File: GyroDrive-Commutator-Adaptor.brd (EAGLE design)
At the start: 127 x 76.2 mm, 24 parts, among them U1 HALL, U2 PCA9517, U3 5V, U4 2.5V, U5 INA2141U, U6 INA2141U, U7 INA2141U, X1 NORCOMP-DB25-SMD-MALE

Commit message: Shortened board by 0.75 inches to make room for DB25-Dale adapter
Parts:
- moved U1 19.0 mm to (102.9, 38.1)
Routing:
- net AGND: track 116.9 -> 97.8 mm
- net HALL0: track 105.4 -> 86.4 mm
- net HALL1: track 109.3 -> 90.6 mm
- net V+_HALL: track 67.0 -> 48.5 mm
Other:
- board size 127 x 76.2 mm -> 108 x 76.2 mm
- board text added: "GyroDrive-Commutator Adapter Version 1 Michael Stetner Fee Lab, 2016"
- board text removed: "Fee lab, 2013"
- board text removed: "Tatsuo Okubo"
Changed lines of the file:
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@@
 <plain>
 <wire x1="0" y1="2.54" x2="2.54" y2="0" width="0" layer="20" curve="90"/>
-<wire x1="2.54" y1="0" x2="48.26" y2="0" width="0" layer="20"/>
-<wire x1="48.26" y1="0" x2="50.8" y2="2.54" width="0" layer="20" curve="90"/>
-<wire x1="50.8" y1="2.54" x2="50.8" y2="27.94" width="0" layer="20"/>
-<wire x1="50.8" y1="27.94" x2="53.34" y2="30.48" width="0" layer="20" curve="-90"/>
-<wire x1="53.34" y1="30.48" x2="124.46" y2="30.48" width="0" layer="20"/>
-<wire x1="124.46" y1="30.48" x2="127" y2="33.02" width="0" layer="20" curve="90"/>
-<wire x1="127" y1="33.02" x2="127" y2="43.18" width="0" layer="20"/>
-<wire x1="127" y1="43.18" x2="124.46" y2="45.72" width="0" layer="20" curve="90"/>
-<wire x1="124.46" y1="45.72" x2="53.34" y2="45.72" width="0" layer="20"/>
-<wire x1="53.34" y1="45.72" x2="50.8" y2="48.26" width="0" layer="20" curve="-90"/>
-<wire x1="50.8" y1="48.26" x2="50.8" y2="73.66" width="0" layer="20"/>
-<wire x1="50.8" y1="73.66" x2="48.26" y2="76.2" width="0" layer="20" curve="90"/>
-<wire x1="48.26" y1="76.2" x2="2.54" y2="76.2" width="0" layer="20"/>
+<wire x1="2.54" y1="0" x2="29.21" y2="0" width="0" layer="20"/>
+<wire x1="29.21" y1="0" x2="31.75" y2="2.54" width="0" layer="20" curve="90"/>
+<wire x1="31.75" y1="2.54" x2="31.75" y2="27.94" width="0" layer="20"/>
+<wire x1="31.75" y1="27.94" x2="34.29" y2="30.48" width="0" layer="20" curve="-90"/>
+<wire x1="34.29" y1="30.48" x2="105.41" y2="30.48" width="0" layer="20"/>
+<wire x1="105.41" y1="30.48" x2="107.95" y2="33.02" width="0" layer="20" curve="90"/>
+<wire x1="107.95" y1="33.02" x2="107.95" y2="43.18" width="0" layer="20"/>
+<wire x1="107.95" y1="43.18" x2="105.41" y2="45.72" width="0" layer="20" curve="90"/>
+<wire x1="105.41" y1="45.72" x2="34.29" y2="45.72" width="0" layer="20"/>
+<wire x1="34.29" y1="45.72" x2="31.75" y2="48.26" width="0" layer="20" curve="-90"/>
+<wire x1="31.75" y1="48.26" x2="31.75" y2="73.66" width="0" layer="20"/>
+<wire x1="31.75" y1="73.66" x2="29.21" y2="76.2" width="0" layer="20" curve="90"/>
+<wire x1="29.21" y1="76.2" x2="2.54" y2="76.2" width="0" layer="20"/>
 <wire x1="2.54" y1="76.2" x2="0" y2="73.66" width="0" layer="20" curve="90"/>
 <wire x1="0" y1="73.66" x2="0" y2="2.54" width="0" layer="20"/>
-<text x="49.53" y="2.54" size="1.778" layer="21" rot="R90">Fee lab, 2013</text>
-<text x="45.72" y="2.54" size="1.778" layer="21" rot="R90">Tatsuo Okubo</text>
+<text x="15.8242" y="42.1386" size="1.778" layer="22" rot="MR270" align="center">GyroDrive-Commutator Adapter
+Version 1
+Michael Stetner
+Fee Lab, 2016</text>
 </plain>
 <attributes>
@@
 </element>
 <element name="X2" library="pinhead" package="2X08" value="" x="27.178" y="38.1" rot="R90"/>
-<element name="U1" library="elm" package="HALL_ON_SIDE" value="HALL" x="121.92" y="38.1"/>
+<element name="U1" library="elm" package="HALL_ON_SIDE" value="HALL" x="102.87" y="38.1"/>
 <element name="U7" library="burr-brown" package="SO16-1" value="INA2141U" x="14.986" y="49.3014" rot="R180">
 <attribute name="OC_NEWARK" value="74C9853" x="-4.064" y="87.4014" size="1.778" layer="27" rot="R180" display="off"/>
@@
 <signal name="HALL0">
 <contactref element="U1" pad="D"/>
-<wire x1="52.07" y1="36.83" x2="118.11" y2="36.83" width="0.3048" layer="1"/>
-<wire x1="118.11" y1="36.83" x2="119.3038" y2="35.6362" width="0.254" layer="1"/>
-<wire x1="119.3038" y1="35.6362" x2="120.396" y2="35.6362" width="0.254" layer="1"/>
+<wire x1="52.07" y1="36.83" x2="99.3902" y2="36.8046" width="0.3048" layer="1"/>
+<wire x1="99.3902" y1="36.8046" x2="100.584" y2="35.6108" width="0.254" layer="1"/>
+<wire x1="100.584" y1="35.6108" x2="101.346" y2="35.6362" width="0.254" layer="1"/>
 <contactref element="U7" pad="16"/>
 <wire x1="52.07" y1="36.83" x2="37.719" y2="36.83" width="0.254" layer="1"/>
@@
 <contactref element="R1" pad="1"/>
 <contactref element="U1" pad="C"/>
-<wire x1="61.595" y1="34.163" x2="121.793" y2="34.163" width="0.3048" layer="1"/>
-<wire x1="121.793" y1="34.163" x2="123.19" y2="35.56" width="0.3048" layer="1"/>
-<wire x1="123.19" y1="35.56" x2="123.571" y2="35.56" width="0.3048" layer="1"/>
-<wire x1="123.571" y1="35.56" x2="123.5964" y2="35.5854" width="0.3048" layer="1"/>
+<wire x1="61.595" y1="34.163" x2="103.0732" y2="34.1376" width="0.3048" layer="1"/>
+<wire x1="103.0732" y1="34.1376" x2="104.4702" y2="35.5346" width="0.3048" layer="1"/>
+<wire x1="104.4702" y1="35.5346" x2="104.8512" y2="35.5346" width="0.3048" layer="1"/>
+<wire x1="104.8512" y1="35.5346" x2="104.5464" y2="35.5854" width="0.3048" layer="1"/>
 <wire x1="61.595" y1="34.163" x2="57.404" y2="34.163" width="0.254" layer="1"/>
 <wire x1="57.404" y1="34.163" x2="57.277" y2="34.29" width="0.254" layer="1"/>
@@
 <contactref element="U1" pad="B"/>
 <contactref element="U7" pad="15"/>
-<wire x1="122.809" y1="38.1" x2="122.809" y2="40.1066" width="0.254" layer="1"/>
-<wire x1="122.809" y1="40.1066" x2="122.1486" y2="40.767" width="0.254" layer="1"/>
-<wire x1="122.1486" y1="40.767" x2="40.3098" y2="40.767" width="0.254" layer="1"/>
+<wire x1="103.759" y1="38.1" x2="104.0892" y2="40.0812" width="0.254" layer="1"/>
+<wire x1="104.0892" y1="40.0812" x2="103.4288" y2="40.7416" width="0.254" layer="1"/>
+<wire x1="103.4288" y1="40.7416" x2="40.3098" y2="40.767" width="0.254" layer="1"/>
 <wire x1="18.1356" y1="44.5516" x2="18.161" y2="44.5262" width="0.254" layer="1"/>
 <via x="40.3098" y="40.767" extent="1-16" drill="0.6"/>
@@
 <contactref element="U7" pad="12"/>
 <contactref element="U5" pad="5"/>
-<wire x1="121.0818" y1="38.1" x2="46.5582" y2="38.1" width="0.254" layer="1"/>
+<wire x1="102.0318" y1="38.1" x2="46.5582" y2="38.1" width="0.254" layer="1"/>
 <polygon width="0.4064" layer="15">
 <vertex x="0" y="0"/>
@@
 <vertex x="29.5656" y="43.18"/>
 <vertex x="29.5656" y="76.2"/>
-<vertex x="50.8" y="76.2"/>
-<vertex x="50.8" y="45.72"/>
-<vertex x="127" y="45.72"/>
-<vertex x="127" y="30.48"/>
-<vertex x="50.8" y="30.48"/>
-<vertex x="50.8" y="0"/>
+<vertex x="31.75" y="76.2"/>
+<vertex x="31.75" y="45.72"/>
+<vertex x="107.95" y="45.72"/>
+<vertex x="107.95" y="30.48"/>
+<vertex x="31.75" y="30.48"/>
+<vertex x="31.75" y="0"/>
 </polygon>
 <contactref element="X1" pad="P$10"/>
@@
 </board>
 </drawing>
+<compatibility>
+<note version="6.3" minversion="6.2.2" severity="warning">
+Since Version 6.2.2 text objects can contain more than one line,
+which will not be processed correctly with this version.
+</note>
+</compatibility>
 </eagle>

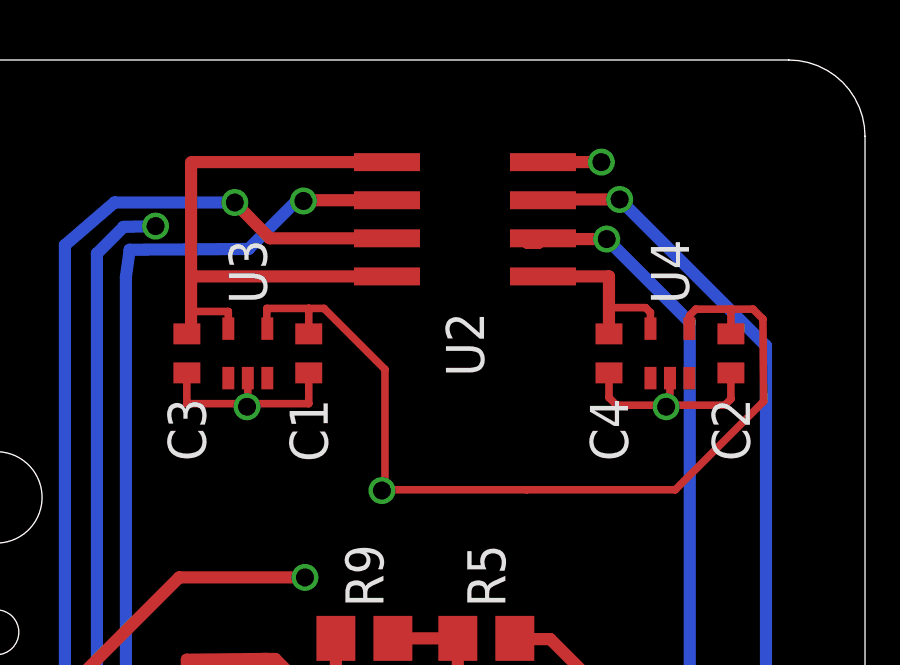
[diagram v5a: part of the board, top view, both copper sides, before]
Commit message: I2C pull-up resistors added
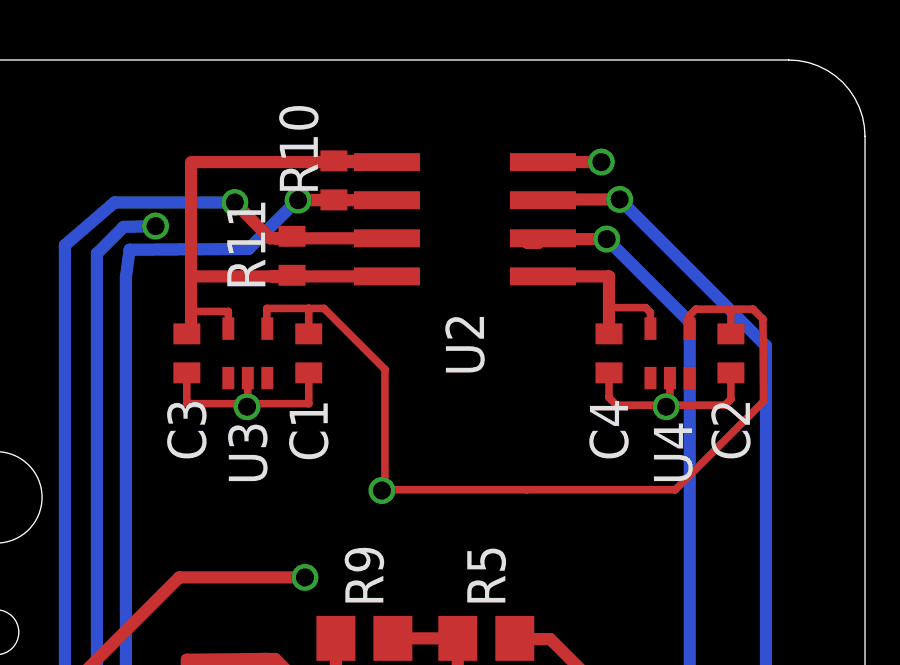
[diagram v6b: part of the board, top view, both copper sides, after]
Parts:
- added R10, R11: 10k, resistor:R0402
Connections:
- net +5V: now also R10.2, R11.2
- net SCL_RIG: now also R11.1
- net SDA_RIG: now also R10.1
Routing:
- net +5V: track 20.7 -> 22.1 mm
- net SDA_RIG: track 50.1 -> 51.3 mm
- net SCL_RIG: track 53.5 -> 54.1 mm
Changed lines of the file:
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@@
 <layer number="27" name="tValues" color="7" fill="1" visible="no" active="yes"/>
 <layer number="28" name="bValues" color="7" fill="1" visible="no" active="yes"/>
-<layer number="29" name="tStop" color="7" fill="3" visible="no" active="yes"/>
+<layer number="29" name="tStop" color="7" fill="3" visible="yes" active="yes"/>
 <layer number="30" name="bStop" color="7" fill="6" visible="yes" active="yes"/>
 <layer number="31" name="tCream" color="7" fill="4" visible="yes" active="yes"/>
@@
 </class>
 </classes>
-<designrules name="OSHPark-4layer">
+<designrules name="OSHPark-4layer *">
 <description language="de">&lt;b&gt;EAGLE Design Rules&lt;/b&gt;
 &lt;p&gt;
@@
 <param name="mlMinCreamFrame" value="0mil"/>
 <param name="mlMaxCreamFrame" value="0mil"/>
-<param name="mlViaStopLimit" value="0mil"/>
+<param name="mlViaStopLimit" value="30mil"/>
 <param name="srRoundness" value="0"/>
 <param name="srMinRoundness" value="0mil"/>
@@
 <element name="X1" library="michael-stetner" package="190-025-163R001" value="NORCOMP-DB25-SMD-MALE" x="0" y="38.1" rot="R90"/>
 <element name="U3" library="michael-stetner" package="SC70" value="5V" x="11.176" y="66.421" smashed="yes">
-<attribute name="NAME" x="11.176" y="68.072" size="1.27" layer="25" rot="R90" align="center-left"/>
+<attribute name="NAME" x="11.176" y="62.0268" size="1.27" layer="25" rot="R90" align="center-left"/>
 <attribute name="VALUE" x="10.414" y="66.167" size="0.4064" layer="27"/>
 </element>
@@
 </element>
 <element name="U4" library="michael-stetner" package="SC70" value="2.5V" x="25.2476" y="66.421" smashed="yes">
-<attribute name="NAME" x="25.2476" y="68.072" size="1.27" layer="25" rot="R90" align="center-left"/>
+<attribute name="NAME" x="25.3492" y="62.0268" size="1.27" layer="25" rot="R90" align="center-left"/>
 <attribute name="VALUE" x="24.4856" y="66.167" size="0.4064" layer="27"/>
 </element>
@@
 <attribute name="NAME" x="23.2156" y="64.9224" size="1.27" layer="25" rot="R270" align="center-left"/>
 <attribute name="VALUE" x="21.3106" y="67.056" size="1.27" layer="27" rot="R270"/>
+</element>
+<element name="R10" library="resistor" package="R0402" value="10k" x="14.0462" y="72.1868" smashed="yes" rot="R90">
+<attribute name="NAME" x="13.5128" y="73.2282" size="1.27" layer="25" rot="R270" align="top-center"/>
+<attribute name="VALUE" x="15.9512" y="71.5518" size="1.27" layer="27" rot="R90"/>
+</element>
+<element name="R11" library="resistor" package="R0402" value="10k" x="12.6492" y="69.6722" smashed="yes" rot="R270">
+<attribute name="NAME" x="11.7602" y="68.5038" size="1.27" layer="25" rot="R90"/>
+<attribute name="VALUE" x="10.7442" y="70.3072" size="1.27" layer="27" rot="R270"/>
 </element>
 </elements>
@@
 <contactref element="U3" pad="5"/>
 <contactref element="C3" pad="1"/>
-<wire x1="15.815" y1="72.7964" x2="9.398" y2="72.7964" width="0.4064" layer="1"/>
+<wire x1="15.815" y1="72.7964" x2="14.7574" y2="72.7964" width="0.4064" layer="1"/>
+<wire x1="14.7574" y1="72.7964" x2="9.398" y2="72.7964" width="0.4064" layer="1"/>
 <wire x1="9.398" y1="72.7964" x2="9.286" y2="72.7964" width="0.4064" layer="1"/>
-<wire x1="15.815" y1="68.9864" x2="9.286" y2="68.9864" width="0.4064" layer="1"/>
+<wire x1="15.815" y1="68.9864" x2="11.9888" y2="68.9864" width="0.4064" layer="1"/>
+<wire x1="11.9888" y1="68.9864" x2="9.286" y2="68.9864" width="0.4064" layer="1"/>
 <wire x1="9.286" y1="68.9864" x2="9.286" y2="72.6844" width="0.4064" layer="1"/>
 <wire x1="9.286" y1="72.6844" x2="9.398" y2="72.7964" width="0.4064" layer="1"/>
@@
 <wire x1="10.526" y1="67.246" x2="10.526" y2="67.818" width="0.254" layer="1"/>
 <wire x1="10.526" y1="67.818" x2="9.286" y2="67.818" width="0.254" layer="1"/>
+<contactref element="R10" pad="2"/>
+<contactref element="R11" pad="2"/>
+<wire x1="14.0462" y1="72.8368" x2="14.7574" y2="72.8368" width="0.4064" layer="1"/>
+<wire x1="14.7574" y1="72.8368" x2="14.7574" y2="72.7964" width="0.4064" layer="1"/>
+<wire x1="12.6492" y1="69.0222" x2="12.6238" y2="68.9714" width="0.4064" layer="1"/>
+<wire x1="12.6238" y1="68.9714" x2="11.9888" y2="68.9864" width="0.4064" layer="1"/>
 </signal>
 <signal name="SDA_BIRD">
@@
 <wire x1="6.1214" y1="33.9344" x2="7.112" y2="33.9344" width="0.4064" layer="16"/>
 <wire x1="7.112" y1="33.9344" x2="7.112" y2="68.961" width="0.4064" layer="16"/>
-<wire x1="15.815" y1="71.5264" x2="13.0556" y2="71.5264" width="0.4064" layer="1"/>
-<wire x1="13.0556" y1="71.5264" x2="13.0302" y2="71.501" width="0.4064" layer="1"/>
-<via x="13.0302" y="71.501" extent="1-16" drill="0.6"/>
-<wire x1="13.0302" y1="71.501" x2="12.8016" y2="71.501" width="0.4064" layer="16"/>
+<wire x1="15.815" y1="71.5264" x2="12.8524" y2="71.5264" width="0.4064" layer="1"/>
+<via x="12.8524" y="71.5264" extent="1-16" drill="0.6"/>
+<wire x1="12.8524" y1="71.5264" x2="12.8016" y2="71.501" width="0.4064" layer="16"/>
 <wire x1="12.8016" y1="71.501" x2="11.2014" y2="69.9008" width="0.4064" layer="16"/>
 <wire x1="11.2014" y1="69.9008" x2="7.239" y2="69.8754" width="0.4064" layer="16"/>
 <wire x1="7.239" y1="69.8754" x2="7.112" y2="68.961" width="0.4064" layer="16"/>
+<contactref element="R10" pad="1"/>
+<wire x1="14.0462" y1="71.5368" x2="13.0302" y2="71.5368" width="0.4064" layer="1"/>
+<wire x1="13.0302" y1="71.5368" x2="12.8524" y2="71.5264" width="0.4064" layer="1"/>
 </signal>
 <signal name="SCL_RIG">
@@
 <wire x1="4.8768" y1="31.1658" x2="5.08" y2="31.1658" width="0.4064" layer="16"/>
 <wire x1="5.08" y1="31.1658" x2="5.08" y2="70.0278" width="0.4064" layer="16"/>
-<wire x1="15.815" y1="70.2564" x2="11.9126" y2="70.2564" width="0.4064" layer="1"/>
+<wire x1="15.815" y1="70.2564" x2="12.0904" y2="70.2564" width="0.4064" layer="1"/>
+<wire x1="12.0904" y1="70.2564" x2="11.9126" y2="70.2564" width="0.4064" layer="1"/>
 <wire x1="11.9126" y1="70.2564" x2="10.7442" y2="71.4502" width="0.4064" layer="1"/>
 <via x="10.7442" y="71.4502" extent="1-16" drill="0.6"/>
 <wire x1="10.7442" y1="71.4502" x2="6.731" y2="71.4502" width="0.4064" layer="16"/>
 <wire x1="6.731" y1="71.4502" x2="5.08" y2="70.0278" width="0.4064" layer="16"/>
+<contactref element="R11" pad="1"/>
+<wire x1="12.6492" y1="70.3222" x2="12.6492" y2="70.246" width="0.4064" layer="1"/>
+<wire x1="12.6492" y1="70.246" x2="12.0904" y2="70.2564" width="0.4064" layer="1"/>
 </signal>
 </signals>
